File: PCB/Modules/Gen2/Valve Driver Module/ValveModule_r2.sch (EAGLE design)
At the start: 23 parts, among them IC1 SN65HVD31DR, IC2 LM3480-5.0, IC3 ISO1H811G, J10 RJ45-8PTH, J8 POWER_JACK

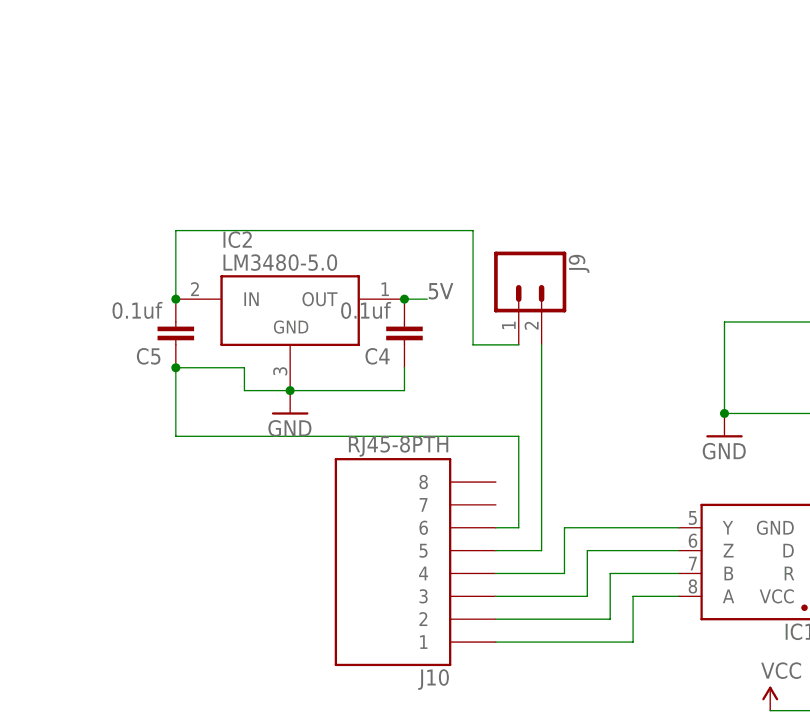
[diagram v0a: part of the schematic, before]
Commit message: -Critical Update for modules with optional RJ45 power (ValveDriver, I2C, SNES and DDS); new PCB designs add a diode to prevent USB power from entering output pin of 5V regulator, when RJ45 (state machine) power is not connected. This update greatly reduces unnecessary power consumption and heat dissipation. If you built a board using the previous designs, please Email a photo of your board to Sanworks support for a free upgrade. -Updated component names on some boards and on web BOMs to avoid skipping parts -Renamed Gen2 module PCB folder from '0.7' to 'Gen2' -Retired pocket state machine (to be replaced with Bpod State Machine r1)
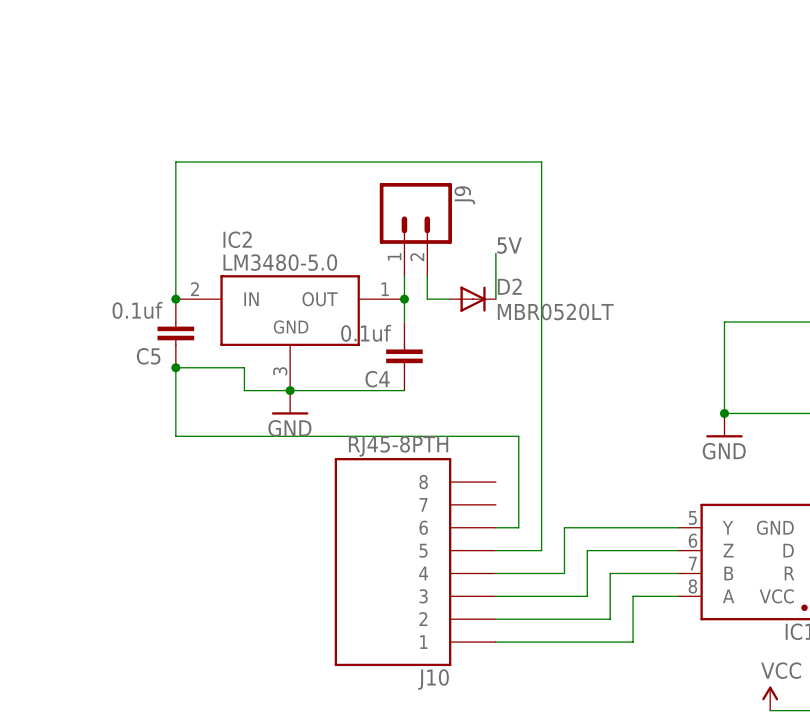
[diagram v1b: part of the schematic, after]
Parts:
- added D2: MBR0520LT, diode:MBR0520LT
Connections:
- new net N$25: C4.2, IC2.OUT, J9.1
- net 5V: now also D2.C; no longer C4.2, IC2.OUT
- net N$24: now also C5.2, IC2.IN; no longer J9.2
- net N$26: now also D2.A, J9.2; no longer C5.2, IC2.IN, J9.1
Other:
- moved on the sheet: C4, J9
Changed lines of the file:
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@@
 <part name="C3" library="JoshParts10" deviceset="EEE-FK1H100UR" device=""/>
 <part name="FRAME1" library="frames" deviceset="A3L-LOC" device=""/>
+<part name="D2" library="diode" deviceset="MBR0520LT" device=""/>
 </parts>
 <sheets>
@@
 <text x="307.086" y="160.274" size="1.778" layer="91">GNDBB</text>
 <text x="320.04" y="205.74" size="1.778" layer="91">GNDBB</text>
-<text x="78.74" y="193.04" size="1.778" layer="97">5V</text>
+<text x="86.36" y="198.12" size="1.778" layer="97">5V</text>
 <wire x1="200.66" y1="248.92" x2="203.2" y2="119.38" width="1.016" layer="94" style="longdash"/>
 <wire x1="-2.54" y1="119.38" x2="203.2" y2="119.38" width="1.016" layer="94" style="longdash"/>
@@
 <instance part="SUPPLY3" gate="G$1" x="269.24" y="210.82"/>
 <instance part="D1" gate="G$1" x="289.56" y="149.86" rot="R180"/>
-<instance part="J9" gate="G$1" x="88.9" y="195.58" rot="R270"/>
+<instance part="J9" gate="G$1" x="76.2" y="203.2" rot="R270"/>
 <instance part="IC2" gate="G$1" x="63.5" y="193.04"/>
-<instance part="C4" gate="G$1" x="76.2" y="190.5" rot="R180"/>
+<instance part="C4" gate="G$1" x="76.2" y="187.96" rot="R180"/>
 <instance part="C5" gate="G$1" x="50.8" y="190.5" rot="R180"/>
 <instance part="GND5" gate="1" x="63.5" y="180.34"/>
 <instance part="C3" gate="G$1" x="304.546" y="154.94" rot="R270"/>
 <instance part="FRAME1" gate="G$1" x="-7.62" y="-7.62"/>
+<instance part="D2" gate="G$1" x="83.82" y="193.04" smashed="yes">
+<attribute name="NAME" x="86.36" y="193.5226" size="1.778" layer="95"/>
+<attribute name="VALUE" x="86.36" y="190.7286" size="1.778" layer="96"/>
+</instance>
 </instances>
 <busses>
@@
 <pinref part="C4" gate="G$1" pin="1"/>
 <wire x1="63.5" y1="182.88" x2="76.2" y2="182.88" width="0.1524" layer="91"/>
-<wire x1="76.2" y1="182.88" x2="76.2" y2="185.42" width="0.1524" layer="91"/>
 <junction x="63.5" y="182.88"/>
 <pinref part="GND5" gate="1" pin="GND"/>
@@
 </segment>
 <segment>
-<pinref part="IC2" gate="G$1" pin="OUT"/>
-<wire x1="76.2" y1="193.04" x2="78.74" y2="193.04" width="0.1524" layer="91"/>
-<pinref part="C4" gate="G$1" pin="2"/>
-<junction x="76.2" y="193.04"/>
+<pinref part="D2" gate="G$1" pin="C"/>
+<wire x1="86.36" y1="193.04" x2="86.36" y2="198.12" width="0.1524" layer="91"/>
 </segment>
 </net>
@@
 <segment>
 <pinref part="J10" gate="G$1" pin="5"/>
-<pinref part="J9" gate="G$1" pin="2"/>
 <wire x1="86.36" y1="165.1" x2="91.44" y2="165.1" width="0.1524" layer="91"/>
-<wire x1="91.44" y1="165.1" x2="91.44" y2="187.96" width="0.1524" layer="91"/>
-</segment>
-</net>
-<net name="N$26" class="0">
-<segment>
-<pinref part="J9" gate="G$1" pin="1"/>
-<wire x1="88.9" y1="187.96" x2="83.82" y2="187.96" width="0.1524" layer="91"/>
-<wire x1="83.82" y1="187.96" x2="83.82" y2="200.66" width="0.1524" layer="91"/>
+<wire x1="91.44" y1="165.1" x2="91.44" y2="208.28" width="0.1524" layer="91"/>
 <pinref part="IC2" gate="G$1" pin="IN"/>
-<wire x1="83.82" y1="200.66" x2="50.8" y2="200.66" width="0.1524" layer="91"/>
-<wire x1="50.8" y1="200.66" x2="50.8" y2="193.04" width="0.1524" layer="91"/>
+<wire x1="91.44" y1="208.28" x2="50.8" y2="208.28" width="0.1524" layer="91"/>
+<wire x1="50.8" y1="208.28" x2="50.8" y2="193.04" width="0.1524" layer="91"/>
 <pinref part="C5" gate="G$1" pin="2"/>
 <junction x="50.8" y="193.04"/>
 </segment>
 </net>
+<net name="N$25" class="0">
+<segment>
+<pinref part="IC2" gate="G$1" pin="OUT"/>
+<pinref part="C4" gate="G$1" pin="2"/>
+<wire x1="76.2" y1="193.04" x2="76.2" y2="190.5" width="0.1524" layer="91"/>
+<pinref part="J9" gate="G$1" pin="1"/>
+<wire x1="76.2" y1="193.04" x2="76.2" y2="195.58" width="0.1524" layer="91"/>
+<junction x="76.2" y="193.04"/>
+</segment>
+</net>
+<net name="N$26" class="0">
+<segment>
+<pinref part="J9" gate="G$1" pin="2"/>
+<wire x1="78.74" y1="195.58" x2="78.74" y2="193.04" width="0.1524" layer="91"/>
+<pinref part="D2" gate="G$1" pin="A"/>
+<wire x1="78.74" y1="193.04" x2="81.28" y2="193.04" width="0.1524" layer="91"/>
+</segment>
+</net>
